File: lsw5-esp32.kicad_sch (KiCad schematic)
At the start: 32 parts, among them J1 Conn_02x03_Odd_Even, J2 Conn_01x04_Pin, J3 USB4105-GF-A, J4 Conn_02x05_Odd_Even, J5 Conn_01x03, Q1 AO3407A, U1 ESP32-S3-WROOM-1U, U2 LD1117S33TR_SOT223, U3 SP3485EN

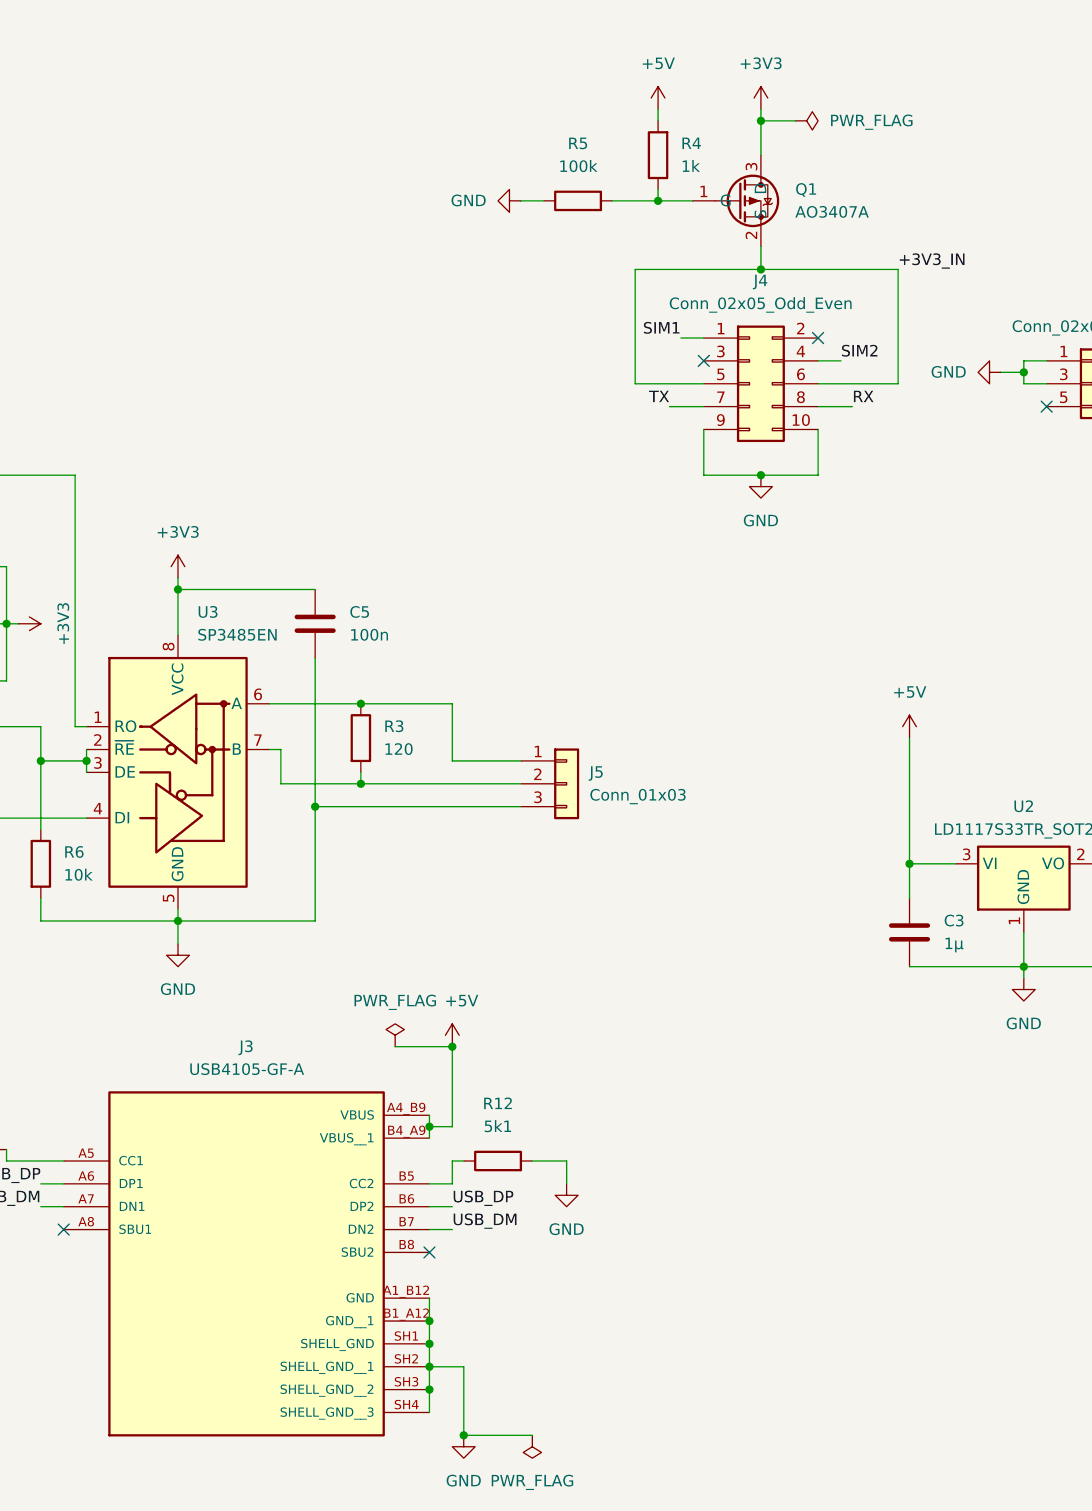
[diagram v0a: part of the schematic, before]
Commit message: Fix fp path, centralise PWR_FLAG
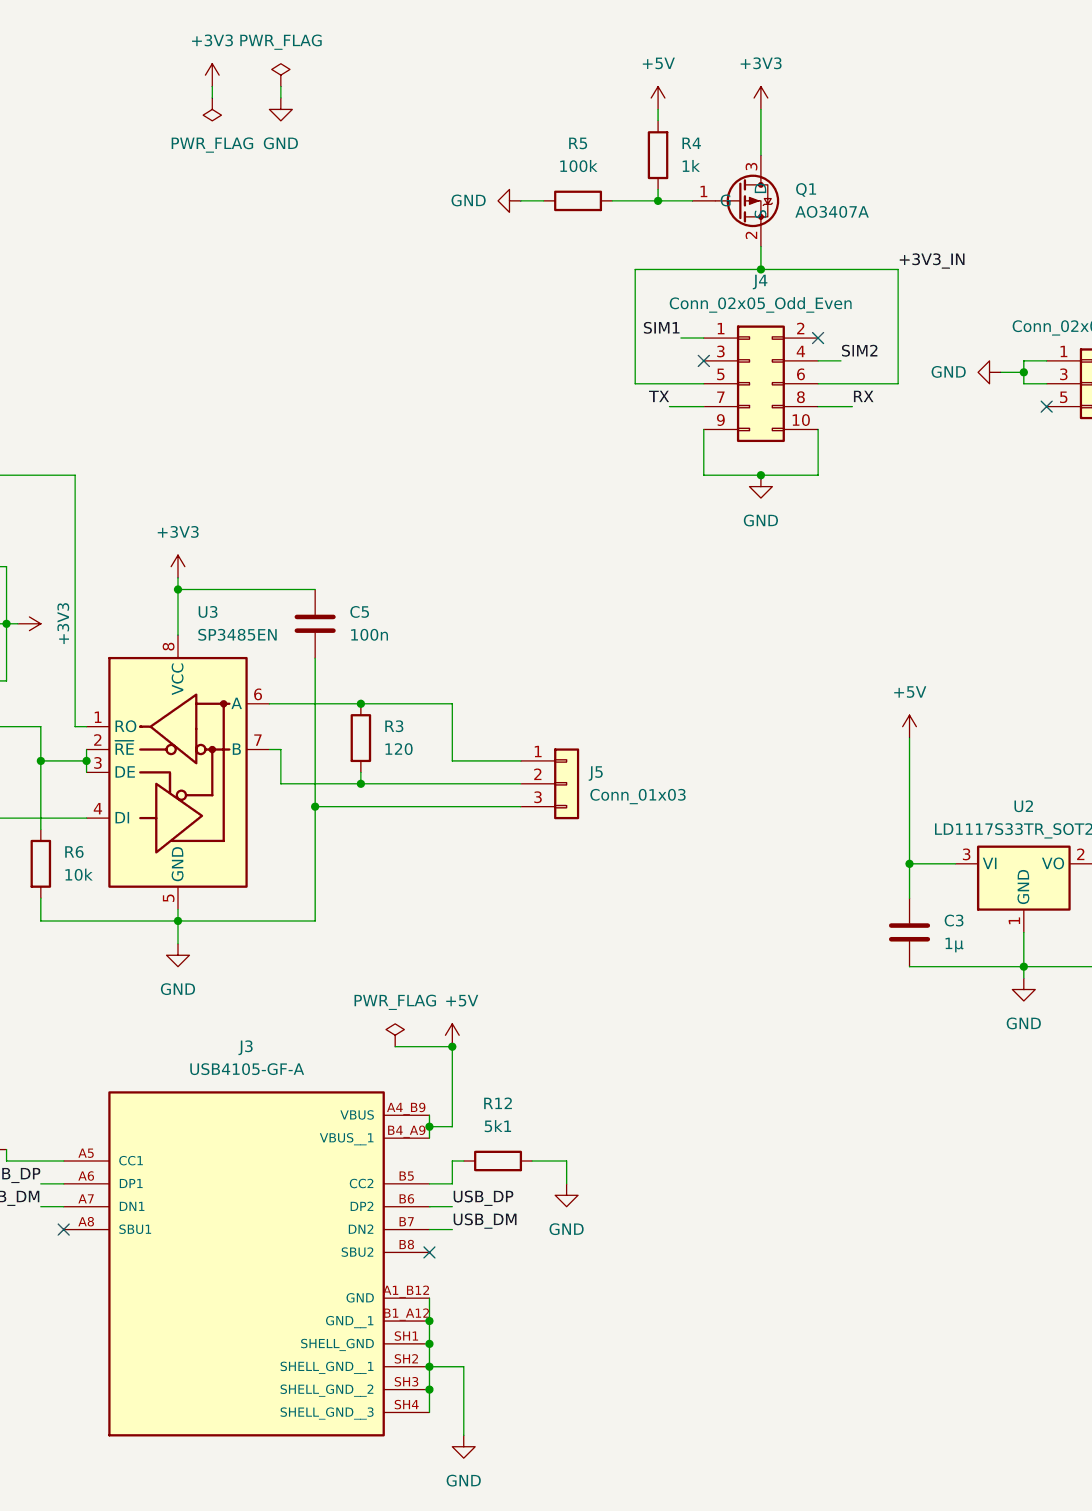
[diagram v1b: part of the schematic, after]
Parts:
- U1: footprint lsw5-esp32:ESP32-S3-WROOM-1U-N16R8 -> ESP32-S3-WROOM-1U:ESP32-S3-WROOM-1U-N16R8

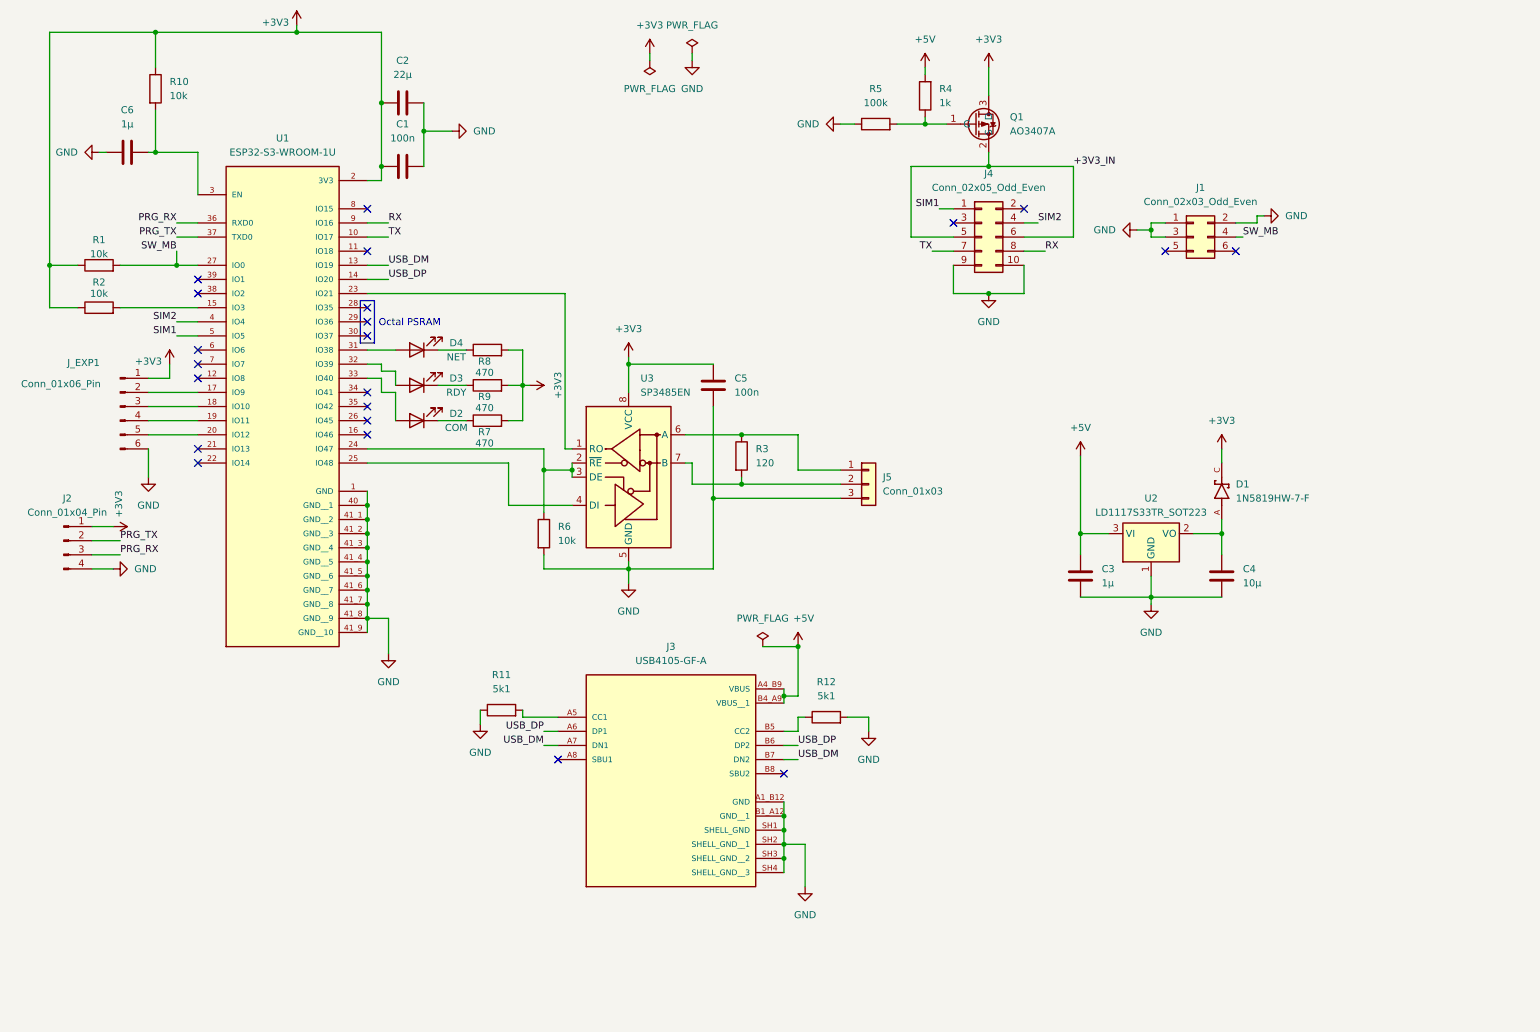
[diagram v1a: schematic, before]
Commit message: p1 isolate RS485 transceiver
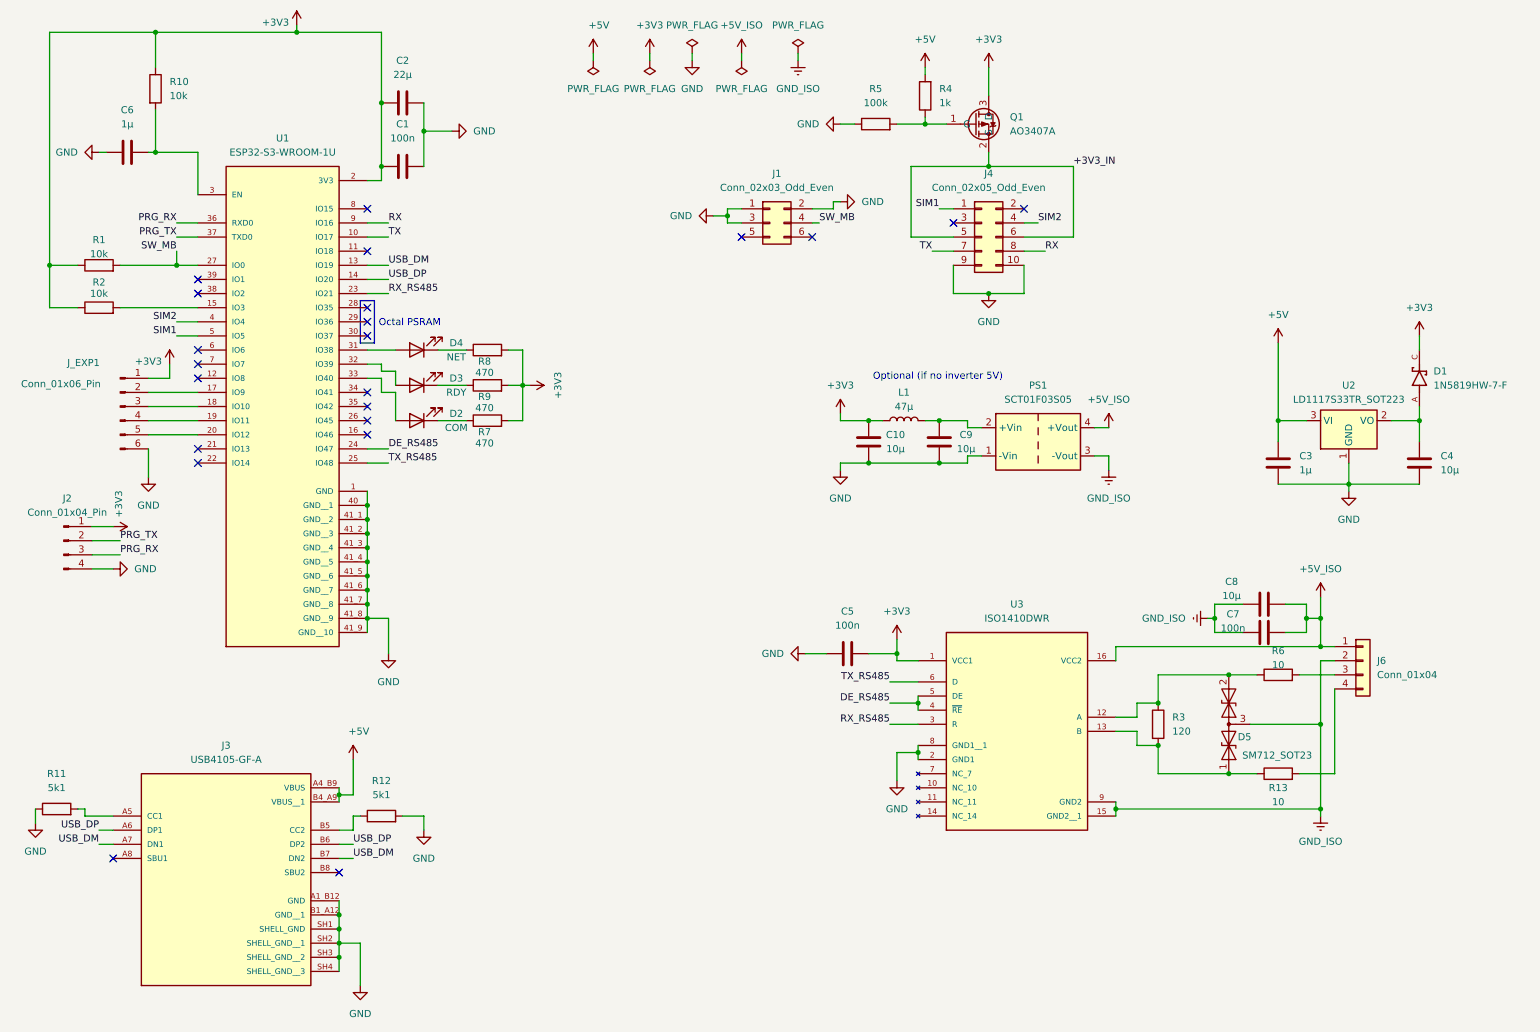
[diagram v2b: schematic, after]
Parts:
- removed J5: Conn_01x03, Connector_PinHeader_2.54mm:PinHeader_1x03_P2.54mm_Vertical, symbol Connector_Generic:Conn_01x03
- removed U3: SP3485EN, Package_SO:SOIC-8_3.9x4.9mm_P1.27mm, symbol Interface_UART:SP3485EN
- added C10, C8, C9: 10μ, Capacitor_SMD:C_0805_2012Metric_Pad1.18x1.45mm_HandSolder, symbol Device:C
- added C7: 100n, Capacitor_SMD:C_0603_1608Metric_Pad1.08x0.95mm_HandSolder, symbol Device:C
- added D5: SM712_SOT23, Package_TO_SOT_SMD:SOT-23, symbol Diode:SM712_SOT23
- added J6: Conn_01x04, Connector_PinHeader_2.54mm:PinHeader_1x04_P2.54mm_Vertical, symbol Connector_Generic:Conn_01x04
- added L1: 47μ, custom-power:L_Ferrocore_DJNR-4018, symbol Device:L
- added PS1: SCT01F03S05, Converter_DCDC:Converter_DCDC_Murata_MEE1SxxxxSC_THT, symbol Converter_DCDC:MEE1S0305SC
- added R13: 10, Resistor_SMD:R_0603_1608Metric_Pad0.98x0.95mm_HandSolder, symbol Device:R
- added U3: ISO1410DWR, ISO1410DWR:SOIC127P1030X265-16N, symbol ISO1410DWR:ISO1410DWR
- R6: value 10k -> 10
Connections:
- net +3V3: now also C10.2, L1.1, U3.1 (VCC1)
- net GND: now also C10.1, C9.1, PS1.1 (-Vin), U3.2 (GND1), U3.8 (GND1__1); no longer R6.2
- net at R3.1: now also R6.1, D5.2 (A2), U3.12 (A)
- net at R3.2: now also D5.1 (A1), R13.1, U3.13 (B)
- net DE_RS485: now reaches U1.24 (IO47)
- net DE_RS485: now also U3.4 (~{RE}), U3.5 (DE); no longer R6.1
- net RX_RS485: now reaches U1.23 (IO21)
- net RX_RS485: now also U3.3 (R)
- net TX_RS485: now reaches U1.25 (IO48)
- net TX_RS485: now also U3.6 (D)
- new net: C9.2, L1.2, PS1.2 (+Vin)
- new net: J6.3 (Pin_3), R6.2
- new net: J6.4 (Pin_4), R13.2
- new net +5V_ISO: C7.1, C8.1, J6.1 (Pin_1), PS1.4 (+Vout), U3.16 (VCC2)
- new net GND_ISO: C7.2, C8.2, D5.3 (common), J6.2 (Pin_2), PS1.3 (-Vout), U3.15 (GND2__1), U3.9 (GND2)
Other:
- note added: "Optional (if no inverter 5V)"
- moved on the sheet: C3, C4, C5, D1, J1, J3, R11, R12, R3, U2

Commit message: set title and revision
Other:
- title: (none) -> LSW5-ESP32
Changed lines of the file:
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@@
 	(generator_version "9.0")
 	(paper "A4")
+	(title_block
+		(title "LSW5-ESP32")
+		(rev "p1")
+	)
 	(rectangle
 		(start 73.66 67.31)

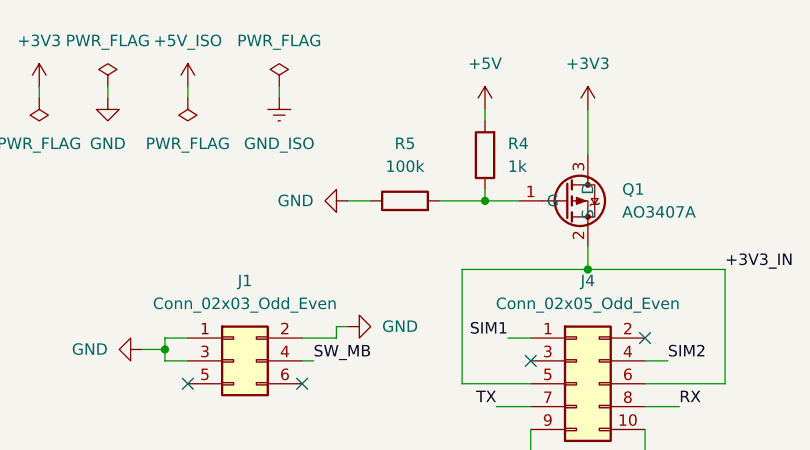
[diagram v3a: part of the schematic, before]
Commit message: improve noise immunity of power switch
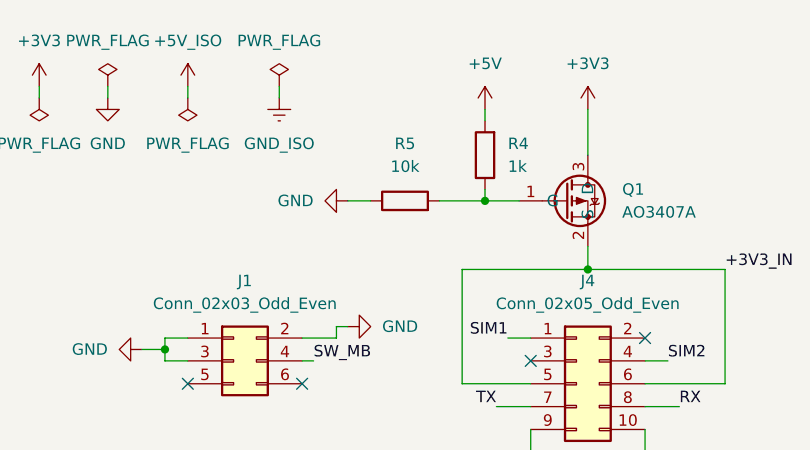
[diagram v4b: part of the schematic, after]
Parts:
- R5: value 100k -> 10k
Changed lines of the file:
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@@
 			)
 		)
-		(property "Value" "100k"
+		(property "Value" "10k"
 			(at 166.37 31.75 90)
 			(effects

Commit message: Fix LED labels on silkscreen
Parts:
- D2: value COM -> NET
- D4: value NET -> COM
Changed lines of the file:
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@@
 	(title_block
 		(title "LSW5-ESP32")
-		(rev "p1")
+		(rev "p2")
 	)
 	(rectangle
@@
 			)
 		)
-		(property "Value" "NET"
+		(property "Value" "COM"
 			(at 90.932 77.47 0)
 			(effects
@@
 			)
 		)
-		(property "Value" "COM"
+		(property "Value" "NET"
 			(at 90.932 90.17 0)
 			(effects

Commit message: RS485 series resistors to 0Ω
To be removed in p2? Also, putting the series resistors before the 120Ω
termination is bad, not that any of these considerations *probably*
matter for chassis wiring
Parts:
- R13, R6: value 10 -> 0
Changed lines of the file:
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@@
 			)
 		)
-		(property "Value" "10"
+		(property "Value" "0"
 			(at 238.76 132.842 90)
 			(effects
@@
 			)
 		)
-		(property "Value" "10"
+		(property "Value" "0"
 			(at 238.76 157.48 90)
 			(effects
